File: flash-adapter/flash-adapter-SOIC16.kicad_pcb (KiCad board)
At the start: 2 copper layers, 11.2 x 11.6 mm, 3 parts, among them J101 Conn_02x04_Odd_Even, U101 W25Q64FVSF

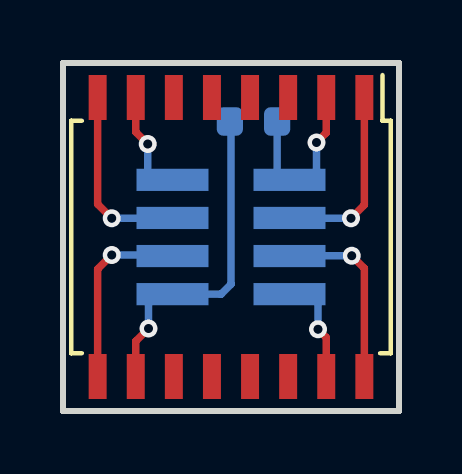
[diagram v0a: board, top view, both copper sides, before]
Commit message: increase trace width
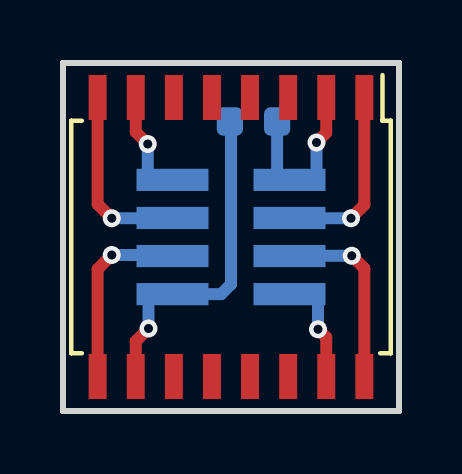
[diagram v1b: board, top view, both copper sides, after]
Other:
- net class Default: trace_width 0.25 -> 0.4
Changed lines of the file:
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@@
   )
   (setup
-    (last_trace_width 0.25)
+    (last_trace_width 0.4)
     (trace_clearance 0.25)
     (zone_clearance 0.508)
@@
   (net_class Default "This is the default net class."
     (clearance 0.25)
-    (trace_width 0.25)
+    (trace_width 0.4)
     (via_dia 0.6)
     (via_drill 0.3)
@@
   (gr_line (start 94.4 94.2) (end 105.6 94.2) (layer Edge.Cuts) (width 0.2))
   (via (at 97.25 103.05) (size 0.6) (drill 0.3) (layers F.Cu B.Cu) (net 1))
-  (segment (start 96.825 103.475) (end 97.25 103.05) (width 0.25) (layer F.Cu) (net 1))
-  (segment (start 96.825 104.65) (end 96.825 103.475) (width 0.25) (layer F.Cu) (net 1))
-  (segment (start 97.445 101.905) (end 98.05 101.905) (width 0.25) (layer B.Cu) (net 1))
-  (segment (start 97.25 102.1) (end 97.445 101.905) (width 0.25) (layer B.Cu) (net 1))
-  (segment (start 97.25 103.05) (end 97.25 102.1) (width 0.25) (layer B.Cu) (net 1))
-  (segment (start 99.67 101.905) (end 98.05 101.905) (width 0.25) (layer B.Cu) (net 1))
-  (segment (start 99.9625 96.2625) (end 100 96.3) (width 0.25) (layer B.Cu) (net 1))
-  (segment (start 100 101.575) (end 99.67 101.905) (width 0.25) (layer B.Cu) (net 1))
-  (segment (start 100 96.3) (end 100 101.575) (width 0.25) (layer B.Cu) (net 1))
-  (segment (start 99.9625 96.15) (end 99.9625 96.2625) (width 0.25) (layer B.Cu) (net 1))
+  (segment (start 96.825 103.475) (end 97.25 103.05) (width 0.4) (layer F.Cu) (net 1))
+  (segment (start 96.825 104.65) (end 96.825 103.475) (width 0.4) (layer F.Cu) (net 1))
+  (segment (start 97.445 101.905) (end 98.05 101.905) (width 0.4) (layer B.Cu) (net 1))
+  (segment (start 97.25 102.1) (end 97.445 101.905) (width 0.4) (layer B.Cu) (net 1))
+  (segment (start 97.25 103.05) (end 97.25 102.1) (width 0.4) (layer B.Cu) (net 1))
+  (segment (start 99.67 101.905) (end 98.05 101.905) (width 0.4) (layer B.Cu) (net 1))
+  (segment (start 99.9625 96.2625) (end 100 96.3) (width 0.4) (layer B.Cu) (net 1))
+  (segment (start 100 101.575) (end 99.67 101.905) (width 0.4) (layer B.Cu) (net 1))
+  (segment (start 100 96.3) (end 100 101.575) (width 0.4) (layer B.Cu) (net 1))
+  (segment (start 99.9625 96.15) (end 99.9625 96.2625) (width 0.4) (layer B.Cu) (net 1))
   (via (at 102.85 96.85) (size 0.6) (drill 0.3) (layers F.Cu B.Cu) (net 2))
-  (segment (start 103.175 96.525) (end 102.85 96.85) (width 0.25) (layer F.Cu) (net 2))
-  (segment (start 103.175 95.35) (end 103.175 96.525) (width 0.25) (layer F.Cu) (net 2))
-  (segment (start 102.605 98.095) (end 101.95 98.095) (width 0.25) (layer B.Cu) (net 2))
-  (segment (start 102.85 97.85) (end 102.605 98.095) (width 0.25) (layer B.Cu) (net 2))
-  (segment (start 102.85 96.85) (end 102.85 97.85) (width 0.25) (layer B.Cu) (net 2))
-  (segment (start 101.5375 98.0875) (end 101.525 98.1) (width 0.25) (layer B.Cu) (net 2))
-  (segment (start 101.5375 96.15) (end 101.5375 98.0875) (width 0.25) (layer B.Cu) (net 2))
+  (segment (start 103.175 96.525) (end 102.85 96.85) (width 0.4) (layer F.Cu) (net 2))
+  (segment (start 103.175 95.35) (end 103.175 96.525) (width 0.4) (layer F.Cu) (net 2))
+  (segment (start 102.605 98.095) (end 101.95 98.095) (width 0.4) (layer B.Cu) (net 2))
+  (segment (start 102.85 97.85) (end 102.605 98.095) (width 0.4) (layer B.Cu) (net 2))
+  (segment (start 102.85 96.85) (end 102.85 97.85) (width 0.4) (layer B.Cu) (net 2))
+  (segment (start 101.5375 98.0875) (end 101.525 98.1) (width 0.4) (layer B.Cu) (net 2))
+  (segment (start 101.5375 96.15) (end 101.5375 98.0875) (width 0.4) (layer B.Cu) (net 2))
   (via (at 97.225 96.9) (size 0.6) (drill 0.3) (layers F.Cu B.Cu) (net 3))
-  (segment (start 96.825 96.5) (end 97.225 96.9) (width 0.25) (layer F.Cu) (net 3))
-  (segment (start 96.825 95.35) (end 96.825 96.5) (width 0.25) (layer F.Cu) (net 3))
-  (segment (start 97.37 98.095) (end 98.05 98.095) (width 0.25) (layer B.Cu) (net 3))
-  (segment (start 97.225 97.95) (end 97.37 98.095) (width 0.25) (layer B.Cu) (net 3))
-  (segment (start 97.225 96.9) (end 97.225 97.95) (width 0.25) (layer B.Cu) (net 3))
+  (segment (start 96.825 96.5) (end 97.225 96.9) (width 0.4) (layer F.Cu) (net 3))
+  (segment (start 96.825 95.35) (end 96.825 96.5) (width 0.4) (layer F.Cu) (net 3))
+  (segment (start 97.37 98.095) (end 98.05 98.095) (width 0.4) (layer B.Cu) (net 3))
+  (segment (start 97.225 97.95) (end 97.37 98.095) (width 0.4) (layer B.Cu) (net 3))
+  (segment (start 97.225 96.9) (end 97.225 97.95) (width 0.4) (layer B.Cu) (net 3))
   (via (at 104 99.375) (size 0.6) (drill 0.3) (layers F.Cu B.Cu) (net 4))
-  (segment (start 104.445 98.93) (end 104 99.375) (width 0.25) (layer F.Cu) (net 4))
-  (segment (start 104.445 95.35) (end 104.445 98.93) (width 0.25) (layer F.Cu) (net 4))
-  (segment (start 101.96 99.375) (end 101.95 99.365) (width 0.25) (layer B.Cu) (net 4))
-  (segment (start 104 99.375) (end 101.96 99.375) (width 0.25) (layer B.Cu) (net 4))
+  (segment (start 104.445 98.93) (end 104 99.375) (width 0.4) (layer F.Cu) (net 4))
+  (segment (start 104.445 95.35) (end 104.445 98.93) (width 0.4) (layer F.Cu) (net 4))
+  (segment (start 101.96 99.375) (end 101.95 99.365) (width 0.4) (layer B.Cu) (net 4))
+  (segment (start 104 99.375) (end 101.96 99.375) (width 0.4) (layer B.Cu) (net 4))
   (via (at 96.025 99.375) (size 0.6) (drill 0.3) (layers F.Cu B.Cu) (net 5))
-  (segment (start 95.555 98.905) (end 96.025 99.375) (width 0.25) (layer F.Cu) (net 5))
-  (segment (start 95.555 95.35) (end 95.555 98.905) (width 0.25) (layer F.Cu) (net 5))
-  (segment (start 98.04 99.375) (end 98.05 99.365) (width 0.25) (layer B.Cu) (net 5))
-  (segment (start 96.025 99.375) (end 98.04 99.375) (width 0.25) (layer B.Cu) (net 5))
-  (segment (start 104.445 101.045) (end 104.025 100.625) (width 0.25) (layer F.Cu) (net 6))
+  (segment (start 95.555 98.905) (end 96.025 99.375) (width 0.4) (layer F.Cu) (net 5))
+  (segment (start 95.555 95.35) (end 95.555 98.905) (width 0.4) (layer F.Cu) (net 5))
+  (segment (start 98.04 99.375) (end 98.05 99.365) (width 0.4) (layer B.Cu) (net 5))
+  (segment (start 96.025 99.375) (end 98.04 99.375) (width 0.4) (layer B.Cu) (net 5))
+  (segment (start 104.445 101.045) (end 104.025 100.625) (width 0.4) (layer F.Cu) (net 6))
   (via (at 104.025 100.625) (size 0.6) (drill 0.3) (layers F.Cu B.Cu) (net 6))
-  (segment (start 104.445 104.65) (end 104.445 101.045) (width 0.25) (layer F.Cu) (net 6))
-  (segment (start 101.96 100.625) (end 101.95 100.635) (width 0.25) (layer B.Cu) (net 6))
-  (segment (start 104.025 100.625) (end 101.96 100.625) (width 0.25) (layer B.Cu) (net 6))
+  (segment (start 104.445 104.65) (end 104.445 101.045) (width 0.4) (layer F.Cu) (net 6))
+  (segment (start 101.96 100.625) (end 101.95 100.635) (width 0.4) (layer B.Cu) (net 6))
+  (segment (start 104.025 100.625) (end 101.96 100.625) (width 0.4) (layer B.Cu) (net 6))
   (via (at 96.025 100.6) (size 0.6) (drill 0.3) (layers F.Cu B.Cu) (net 7))
-  (segment (start 95.555 101.07) (end 96.025 100.6) (width 0.25) (layer F.Cu) (net 7))
-  (segment (start 95.555 104.65) (end 95.555 101.07) (width 0.25) (layer F.Cu) (net 7))
-  (segment (start 98.015 100.6) (end 98.05 100.635) (width 0.25) (layer B.Cu) (net 7))
-  (segment (start 96.025 100.6) (end 98.015 100.6) (width 0.25) (layer B.Cu) (net 7))
+  (segment (start 95.555 101.07) (end 96.025 100.6) (width 0.4) (layer F.Cu) (net 7))
+  (segment (start 95.555 104.65) (end 95.555 101.07) (width 0.4) (layer F.Cu) (net 7))
+  (segment (start 98.015 100.6) (end 98.05 100.635) (width 0.4) (layer B.Cu) (net 7))
+  (segment (start 96.025 100.6) (end 98.015 100.6) (width 0.4) (layer B.Cu) (net 7))
   (via (at 102.9 103.075) (size 0.6) (drill 0.3) (layers F.Cu B.Cu) (net 8))
-  (segment (start 103.175 103.35) (end 102.9 103.075) (width 0.25) (layer F.Cu) (net 8))
-  (segment (start 103.175 104.65) (end 103.175 103.35) (width 0.25) (layer F.Cu) (net 8))
-  (segment (start 102.9 102.125) (end 102.68 101.905) (width 0.25) (layer B.Cu) (net 8))
-  (segment (start 102.68 101.905) (end 101.95 101.905) (width 0.25) (layer B.Cu) (net 8))
-  (segment (start 102.9 103.075) (end 102.9 102.125) (width 0.25) (layer B.Cu) (net 8))
+  (segment (start 103.175 103.35) (end 102.9 103.075) (width 0.4) (layer F.Cu) (net 8))
+  (segment (start 103.175 104.65) (end 103.175 103.35) (width 0.4) (layer F.Cu) (net 8))
+  (segment (start 102.9 102.125) (end 102.68 101.905) (width 0.4) (layer B.Cu) (net 8))
+  (segment (start 102.68 101.905) (end 101.95 101.905) (width 0.4) (layer B.Cu) (net 8))
+  (segment (start 102.9 103.075) (end 102.9 102.125) (width 0.4) (layer B.Cu) (net 8))
 )

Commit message: update pad to mask clearance
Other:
- rule pad_to_mask_clearance: 0.2 -> 0.1
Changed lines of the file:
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@@
     (pad_size 1.524 1.524)
     (pad_drill 0.762)
-    (pad_to_mask_clearance 0.2)
+    (pad_to_mask_clearance 0.1)
     (aux_axis_origin 0 0)
     (visible_elements FFFFFF7F)
